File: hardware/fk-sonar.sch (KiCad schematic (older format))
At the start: 80 parts, among them J1 Conn_01x03, J2 CONN-HDR-2x5, J3 RF-SMA-EDGE, J4 MICRO-USB, J5 S2B-PH-SM4-TB, J6 Conn_01x04, J7 S2B-PH-SM4-TB, J8 Conn_01x03, M1 MOUNT_HOLE, M2 FIDUCIAL, M3 MOUNT_HOLE, M4 MOUNT_HOLE, M5 FIDUCIAL, M6 MOUNT_HOLE, Q1 2N7002LT1G, Q2 2N7002LT1G, Q3 2N7002LT1G, Q4 2N7002LT1G, SW1 SPNO, U1 ATSAMD21G18A-AU, U2 RFM95W, U3 BQ24074RGTT, U4 S25FL116K0XMFI041, U5 MAX1704XX, U6 MCP1700T-3302E/MB, Y1 FC-135

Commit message: Updating BOM details.
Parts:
- J8: spn1 (none) -> 538-502382-0370
- R21, R22: spn1 603-RC0603FR-07180RL -> 603-AF0603JR-074K7L

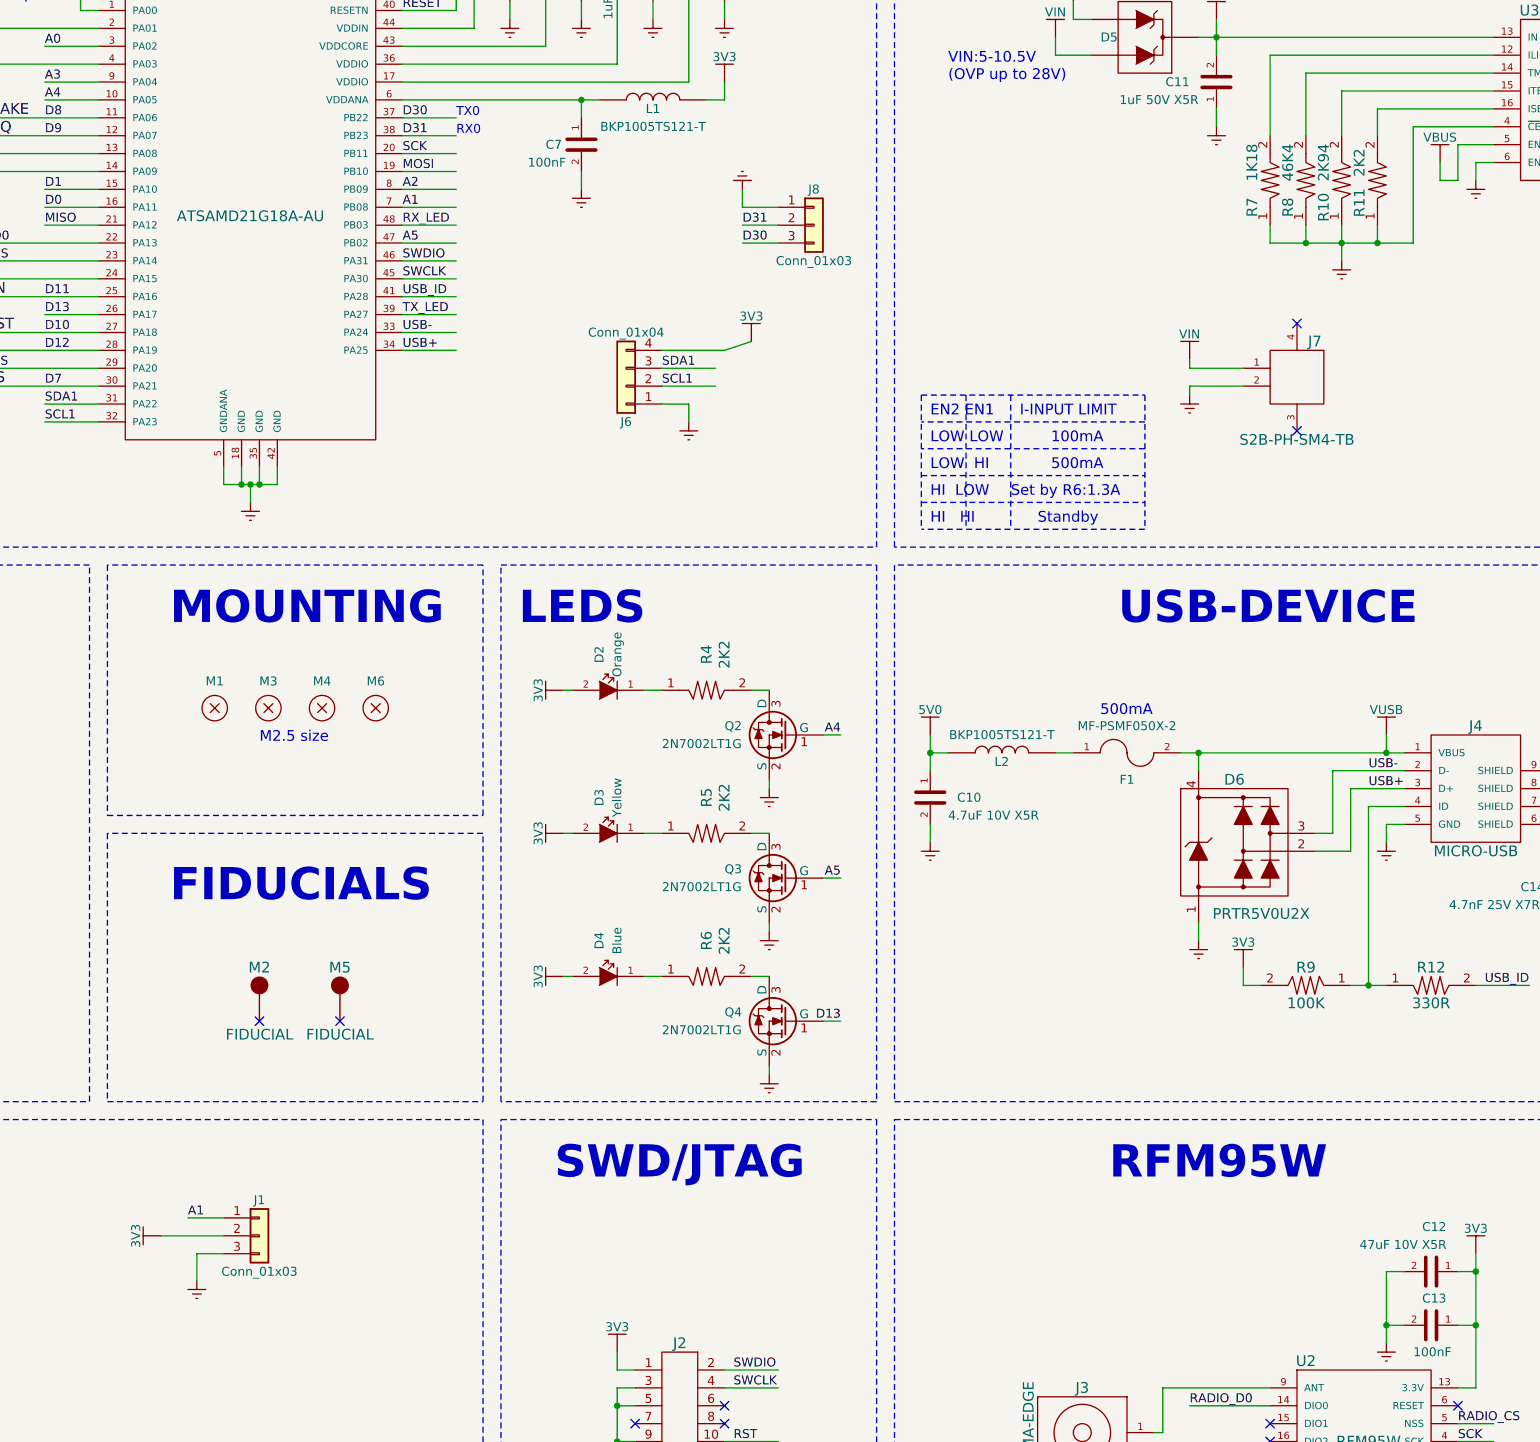
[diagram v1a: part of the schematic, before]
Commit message: Change orientation of sonar sensor connector. Matches the harness we have.
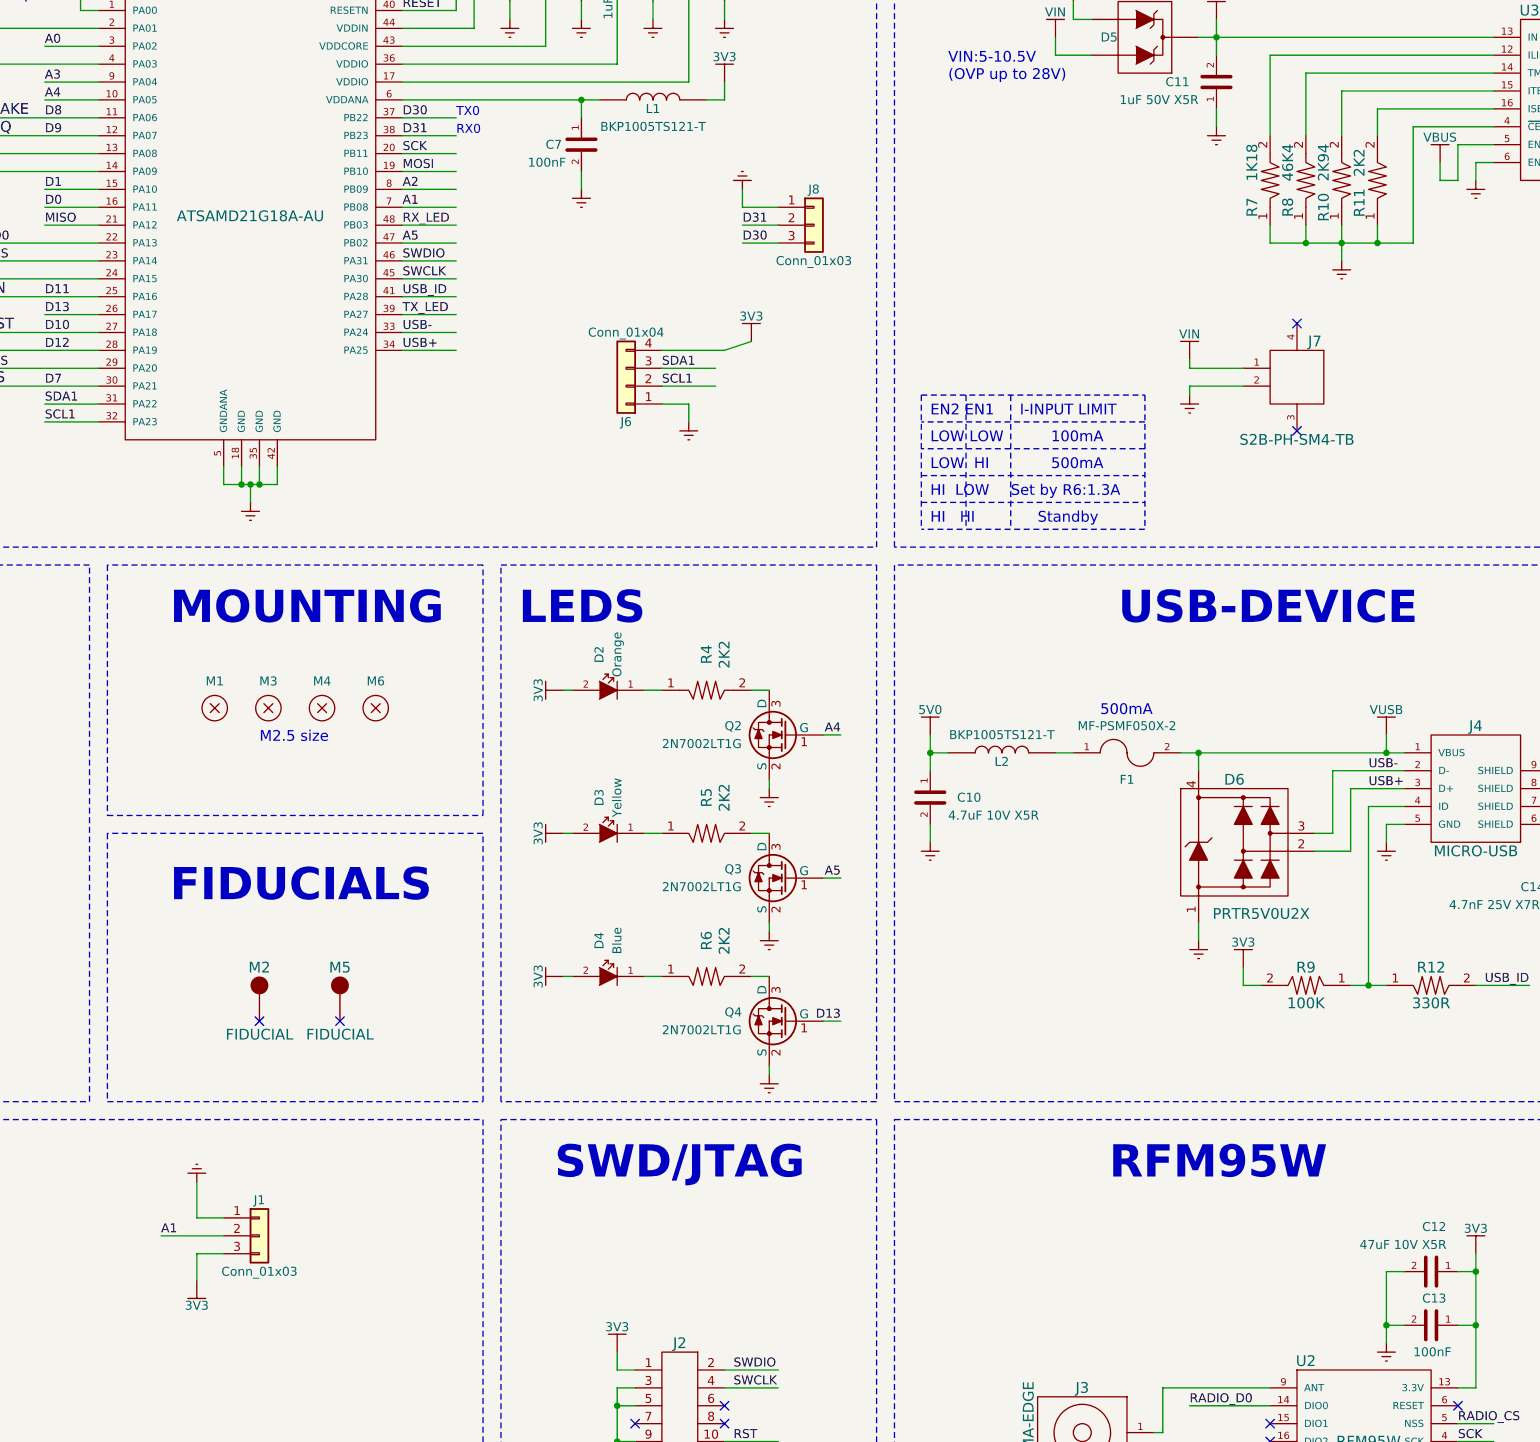
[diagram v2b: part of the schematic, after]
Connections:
- wire segments 292 -> 293

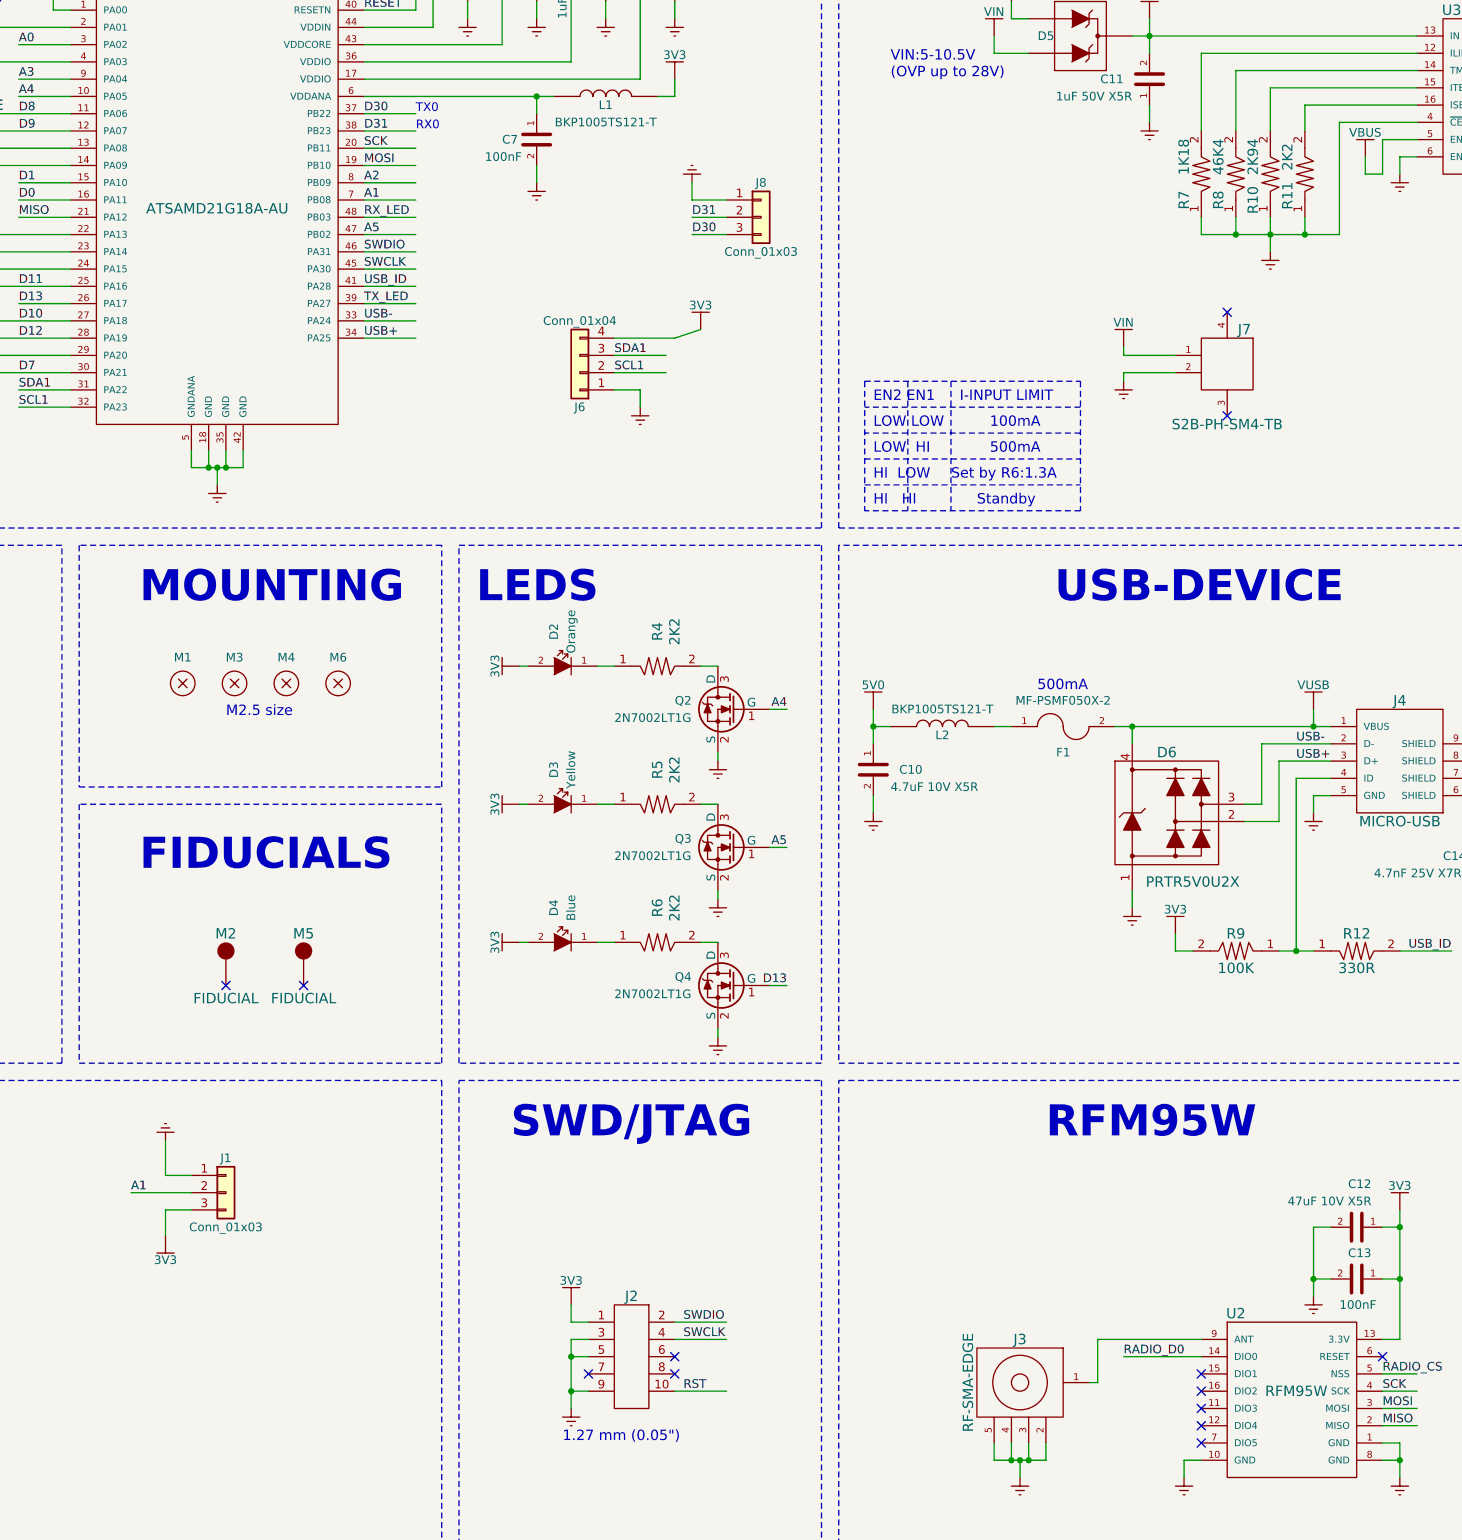
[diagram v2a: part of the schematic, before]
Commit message: Adding main connector and mounting holes. Bump version to v0.3
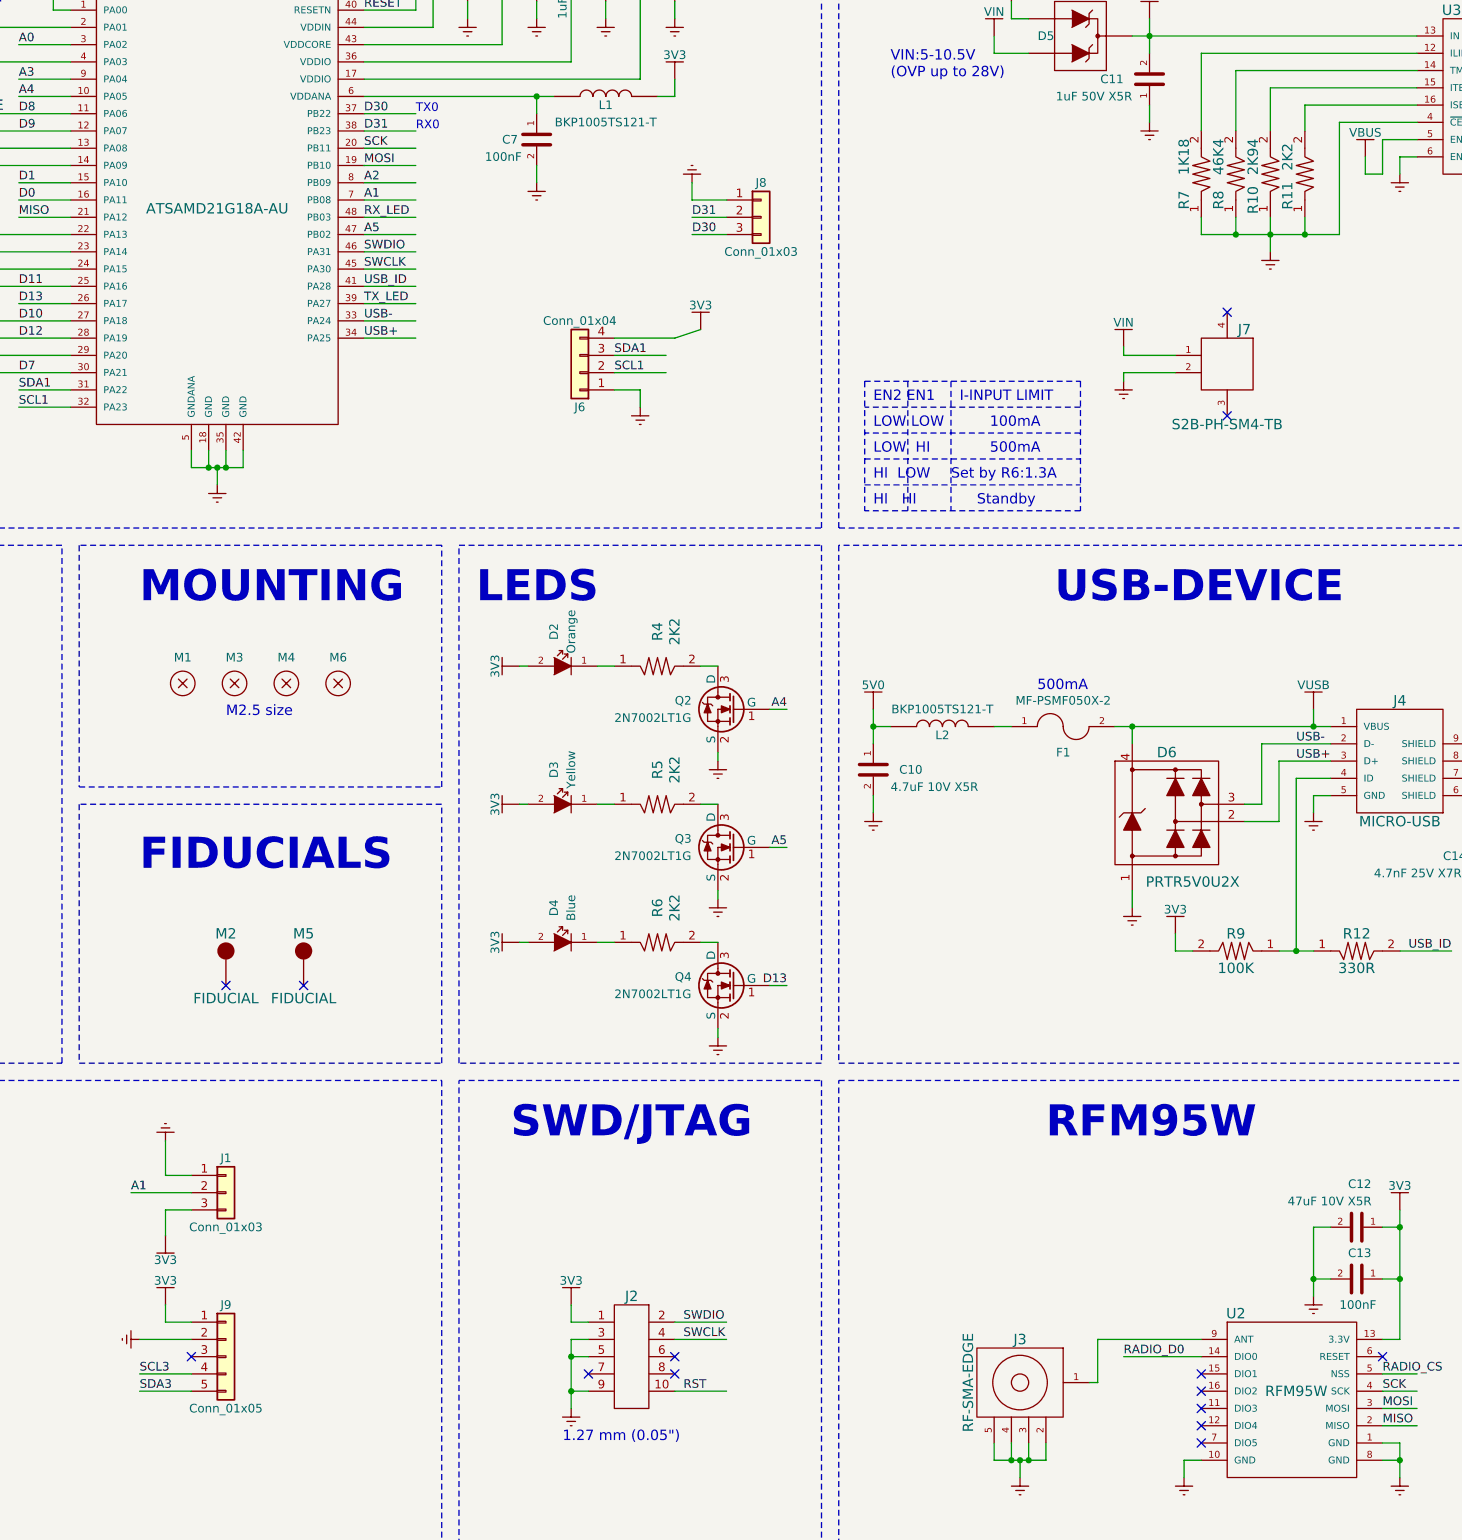
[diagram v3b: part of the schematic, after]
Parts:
- added J9: Conn_01x05, conservify:Molex_CLIK-Mate_502386-0570_1x05_P1.25mm_Horizontal, symbol Conn_01x05
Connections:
- wire segments 293 -> 298
- no-connect marks 19 -> 20
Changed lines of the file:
@@
 	10600 2750 10150 2750
 Wire Wire Line
-	10150 3400 10150 2750
-Wire Wire Line
-	9350 3400 10150 3400
+	10150 2750 10150 3400
+Wire Wire Line
+	10150 3400 9350 3400
 Wire Wire Line
 	9950 3400 9950 3300
@@
 Wire Wire Line
 	3350 8650 3350 8850
+$Comp
+L Conn_01x05 J9
+U 1 1 5B3C0E98
+P 3700 9900
+F 0 "J9" H 3700 10200 50  0000 C CNN
+F 1 "Conn_01x05" H 3700 9600 50  0000 C CNN
+F 2 "conservify:Molex_CLIK-Mate_502386-0570_1x05_P1.25mm_Horizontal" H 3700 9900 50  0001 C CNN
+F 3 "" H 3700 9900 50  0001 C CNN
+	1    3700 9900
+	1    0    0    -1
+$EndComp
+$Comp
+L 3V3 #PWR076
+U 1 1 5B3C1232
+P 3350 9600
+F 0 "#PWR076" H 3350 9450 50  0001 C CNN
+F 1 "3V3" H 3350 9740 50  0000 C CNN
+F 2 "" H 3350 9600 60  0000 C CNN
+F 3 "" H 3350 9600 60  0000 C CNN
+	1    3350 9600
+	1    0    0    -1
+$EndComp
+$Comp
+L GND #PWR077
+U 1 1 5B3C1330
+P 3200 9800
+F 0 "#PWR077" H 3200 9550 50  0001 C CNN
+F 1 "GND" H 3200 9650 50  0001 C CNN
+F 2 "" H 3200 9800 60  0000 C CNN
+F 3 "" H 3200 9800 60  0000 C CNN
+	1    3200 9800
+	0    1    1    0
+$EndComp
+NoConn ~ 3500 9900
+Text Label 3200 10100 0    50   ~ 0
+SDA3
+Text Label 3200 10000 0    50   ~ 0
+SCL3
+Wire Wire Line
+	3200 10000 3500 10000
+Wire Wire Line
+	3500 10100 3200 10100
+Wire Wire Line
+	3200 9800 3500 9800
+Wire Wire Line
+	3350 9600 3350 9700
+Wire Wire Line
+	3350 9700 3500 9700
 $EndSCHEMATC
